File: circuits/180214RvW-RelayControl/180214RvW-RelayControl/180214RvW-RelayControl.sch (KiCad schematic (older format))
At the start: 11 parts, among them J1 Barrel_Jack_Switch, J2 Screw_Terminal_01x02, J3 Screw_Terminal_01x03, K1 G6E, Q1 BC549, U1 LM317_TO3

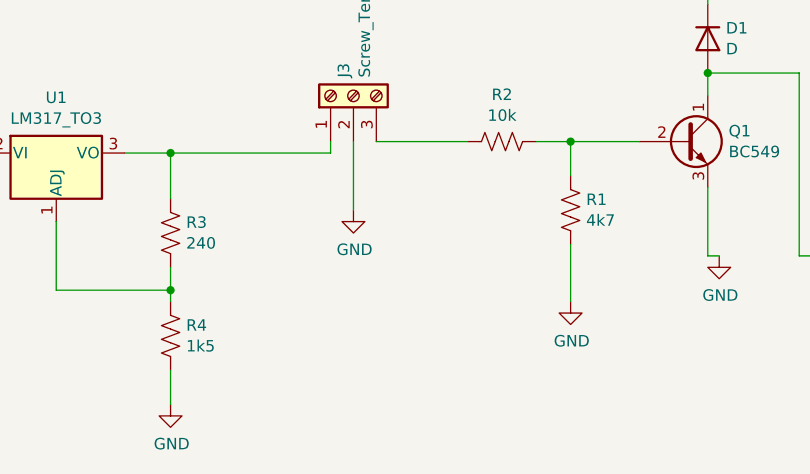
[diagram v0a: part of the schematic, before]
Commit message: Relay Control board complete
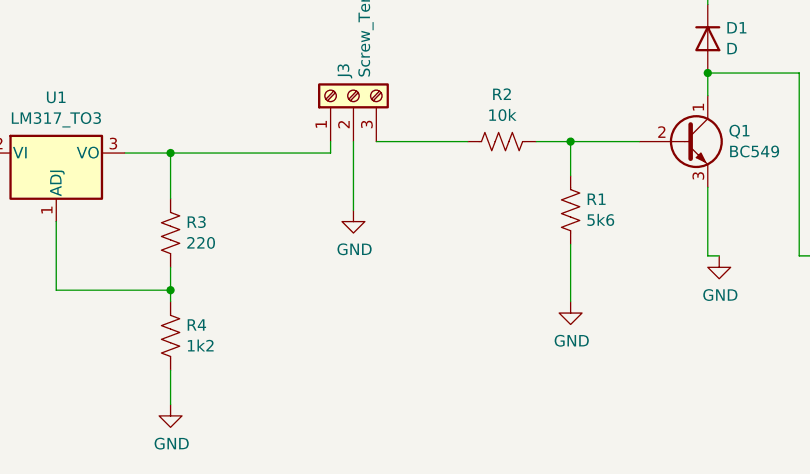
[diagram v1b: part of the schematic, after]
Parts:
- R1: value 4k7 -> 5k6
- R3: value 240 -> 220
- R4: value 1k5 -> 1k2
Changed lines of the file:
@@
 EESchema Schematic File Version 4
+LIBS:180214RvW-RelayControl-cache
 EELAYER 30 0
 EELAYER END
@@
 P 3750 3350
 F 0 "R4" H 3818 3396 50  0000 L CNN
-F 1 "1k5" H 3818 3305 50  0000 L CNN
+F 1 "1k2" H 3818 3305 50  0000 L CNN
 F 2 "Resistor_THT:R_Axial_DIN0411_L9.9mm_D3.6mm_P20.32mm_Horizontal" V 3790 3340 50  0001 C CNN
 F 3 "~" H 3750 3350 50  0001 C CNN
@@
 P 3750 2900
 F 0 "R3" H 3818 2946 50  0000 L CNN
-F 1 "240" H 3818 2855 50  0000 L CNN
+F 1 "220" H 3818 2855 50  0000 L CNN
 F 2 "Resistor_THT:R_Axial_DIN0411_L9.9mm_D3.6mm_P20.32mm_Horizontal" V 3790 2890 50  0001 C CNN
 F 3 "~" H 3750 2900 50  0001 C CNN
@@
 P 5500 2800
 F 0 "R1" H 5568 2846 50  0000 L CNN
-F 1 "4k7" H 5568 2755 50  0000 L CNN
+F 1 "5k6" H 5568 2755 50  0000 L CNN
 F 2 "Resistor_THT:R_Axial_DIN0411_L9.9mm_D3.6mm_P20.32mm_Horizontal" V 5540 2790 50  0001 C CNN
 F 3 "~" H 5500 2800 50  0001 C CNN

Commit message: Updating explanation
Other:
- note added: "Vout = Vref*(1+R3/R4) \n = 1.25*(1+1200/220)\n = 8 V"
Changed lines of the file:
@@
 EESchema Schematic File Version 4
-LIBS:180214RvW-RelayControl-cache
 EELAYER 30 0
 EELAYER END
@@
 Wire Wire Line
 	1050 3250 1050 3500
+Text Notes 2450 4850 0    197  ~ 0
+Vout = Vref*(1+R3/R4) \n         = 1.25*(1+1200/220)\n         = 8 V
 $EndSCHEMATC
